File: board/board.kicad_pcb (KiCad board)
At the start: 2 copper layers, 41 parts, among them J2 Conn_01x10, J3 Conn_01x06, J4 Conn_01x02, J7 Conn_01x30, J8 USB_C_Receptacle_USB2.0_16P, J9 Conn_01x02, U2 nPM1300-QEAA, U3 MDBT50Q-P1MV2, U4 TVS_Array, Y1 32k Hz

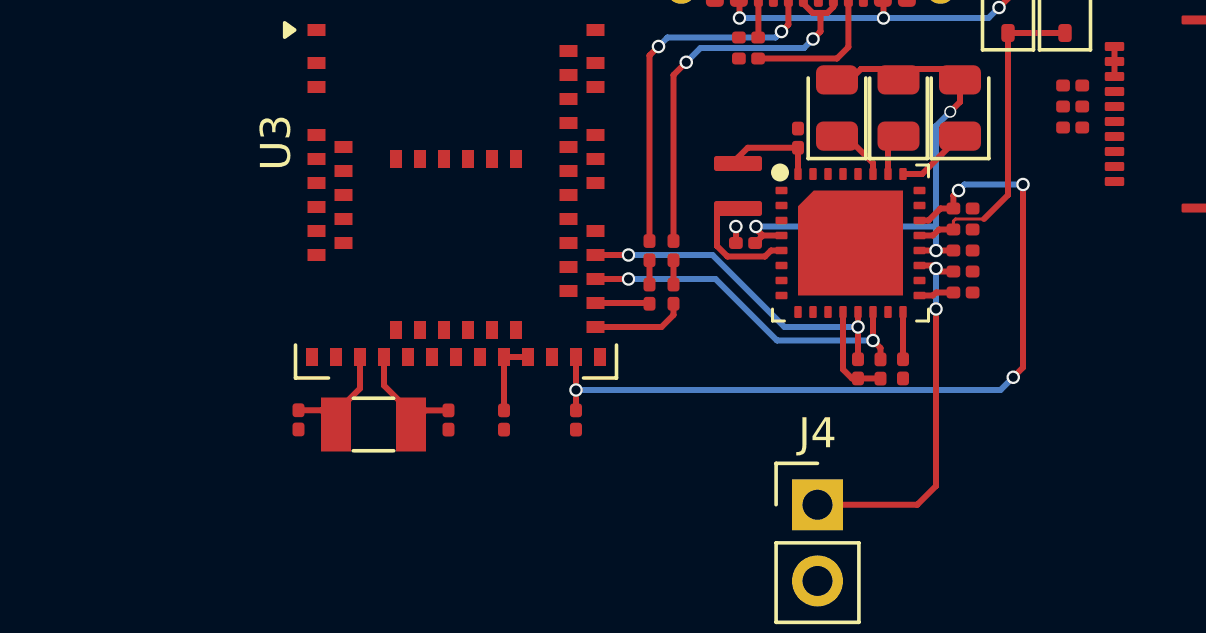
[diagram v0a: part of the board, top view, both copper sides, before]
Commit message: board: pcb move components and traces extending over the edge
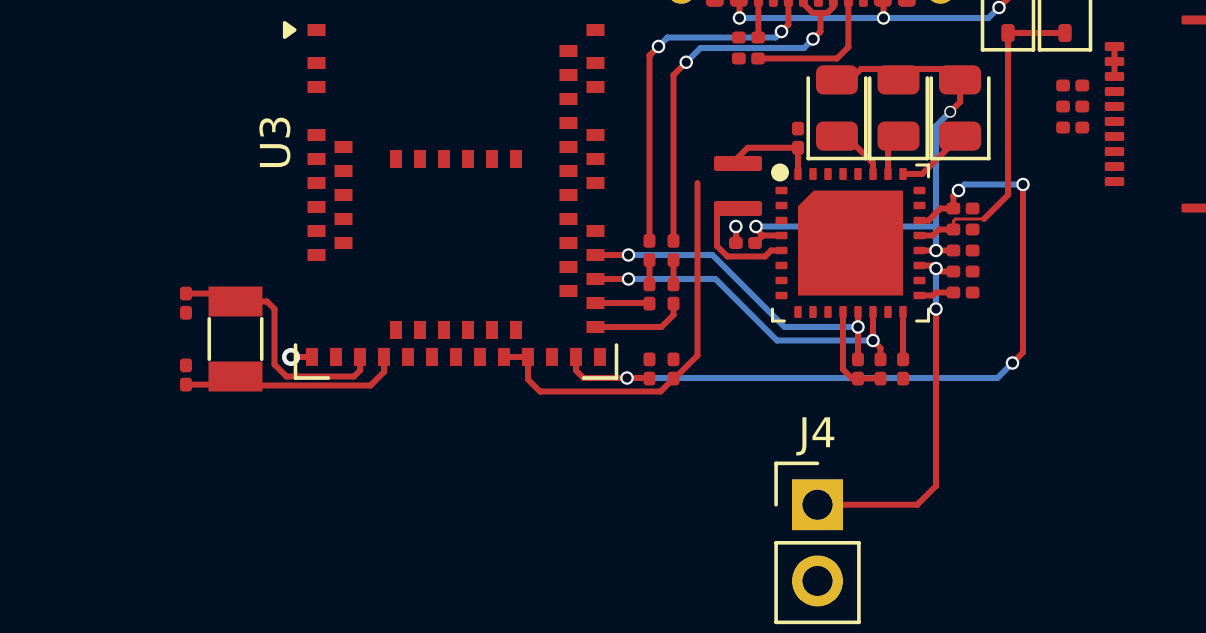
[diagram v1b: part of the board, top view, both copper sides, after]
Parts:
- moved C7 8.88 mm to (90.8, 65.7), turned to 90 degrees
- moved C10 5.90 mm to (107.1, 65.5), turned to -90 degrees
- moved Y1 5.41 mm to (92.5, 64.5), turned to 90 degrees
- moved C8 5.40 mm to (90.8, 63.3)
- moved C9 2.98 mm to (106.3, 65.5), turned to 90 degrees
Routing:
- net +3V3: track 9.22 -> 20.3 mm
- net Net-(U3-P0.00): track 4.03 -> 8.56 mm
- net Net-(U3-P0.01): track 4.07 -> 7.15 mm
- net vbus: track 27.3 -> 26.4 mm
- net GND: track 1.56 -> 2.26 mm, vias 1 -> 2

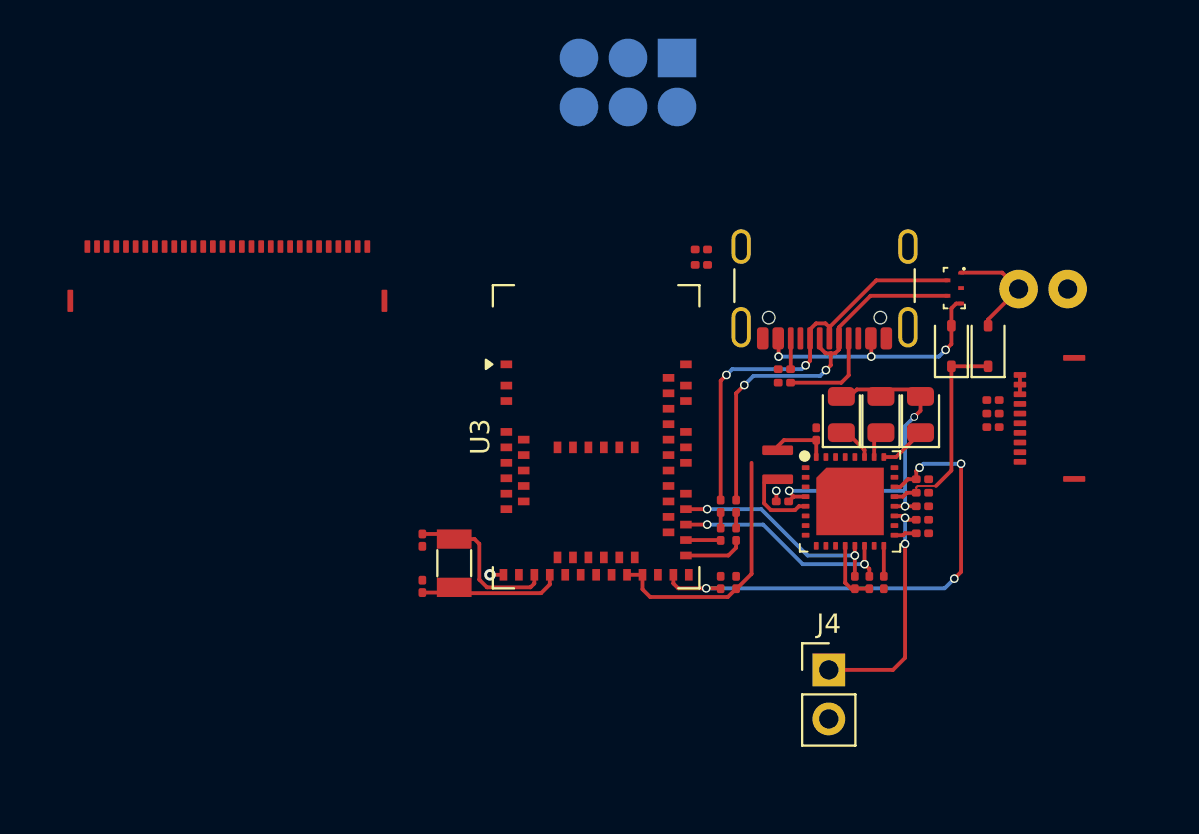
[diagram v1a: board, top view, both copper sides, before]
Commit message: board: pcb add edge cuts
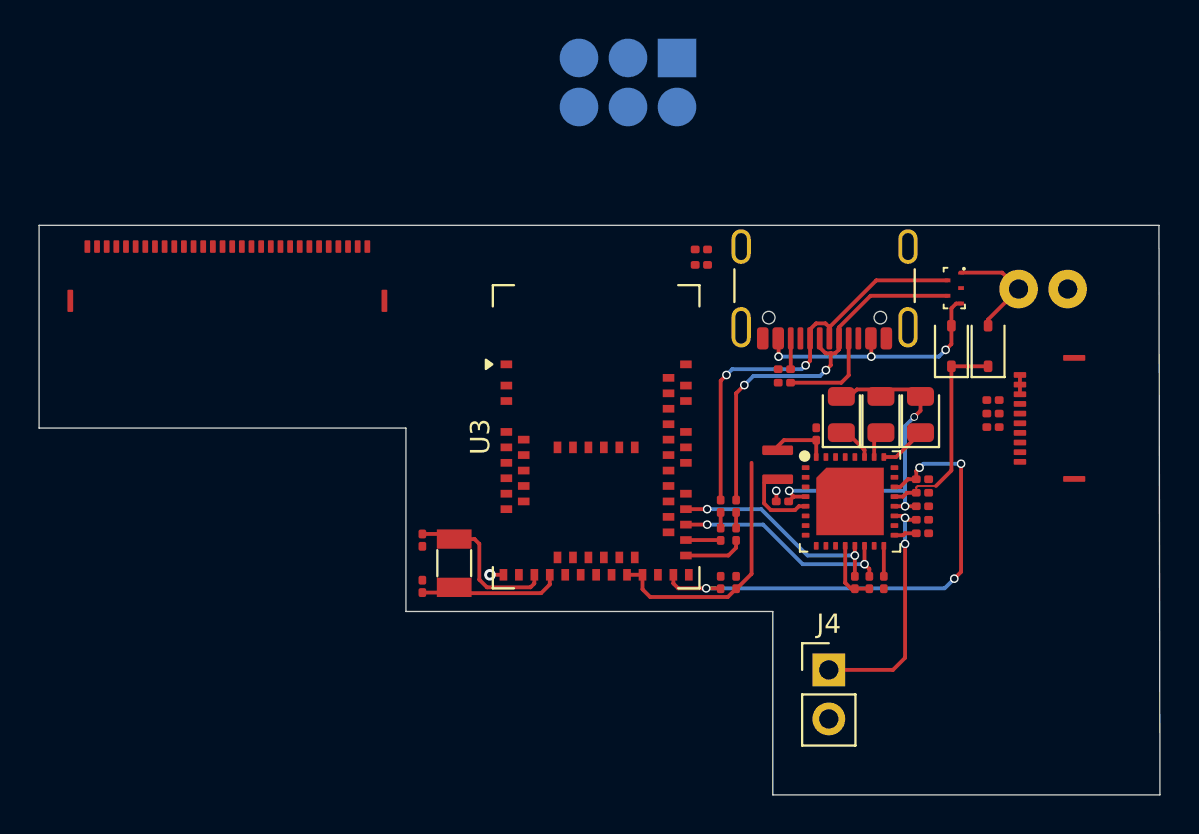
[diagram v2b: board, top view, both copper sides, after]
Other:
- board outline added: 58.1 x 29.5 mm
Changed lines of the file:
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@@
 		(embedded_fonts no)
+	)
+	(gr_poly
+		(pts
+			(xy 71 47) (xy 71 57.5) (xy 90 57.5) (xy 90 67) (xy 109 67) (xy 109 76.5) (xy 129.05 76.5) (xy 129 47)
+		)
+		(stroke
+			(width 0.05)
+			(type solid)
+		)
+		(fill no)
+		(layer "Edge.Cuts")
 	)
 	(gr_line

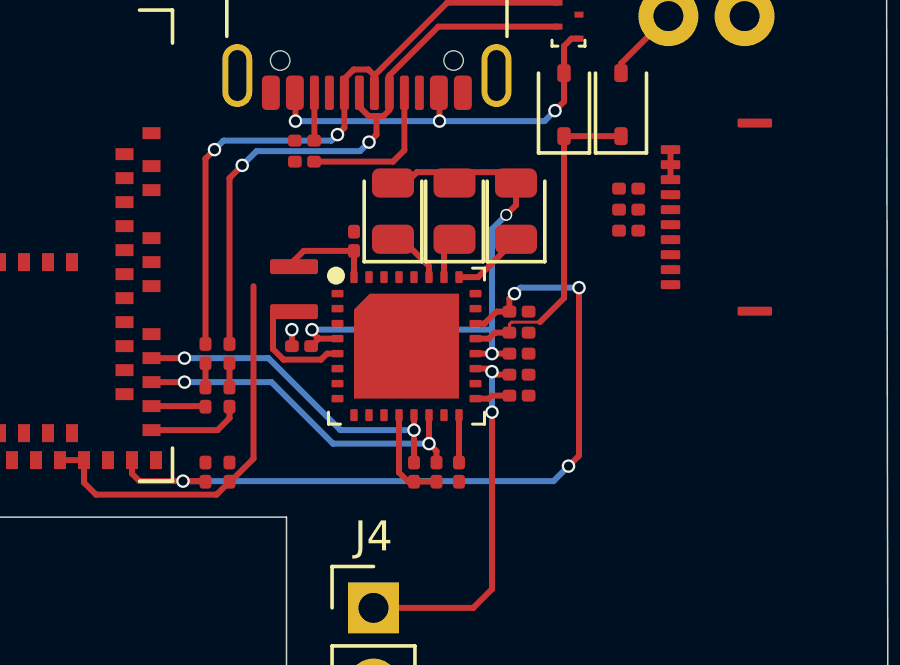
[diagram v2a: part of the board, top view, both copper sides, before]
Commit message: board: pcb route (most of) 3.3V
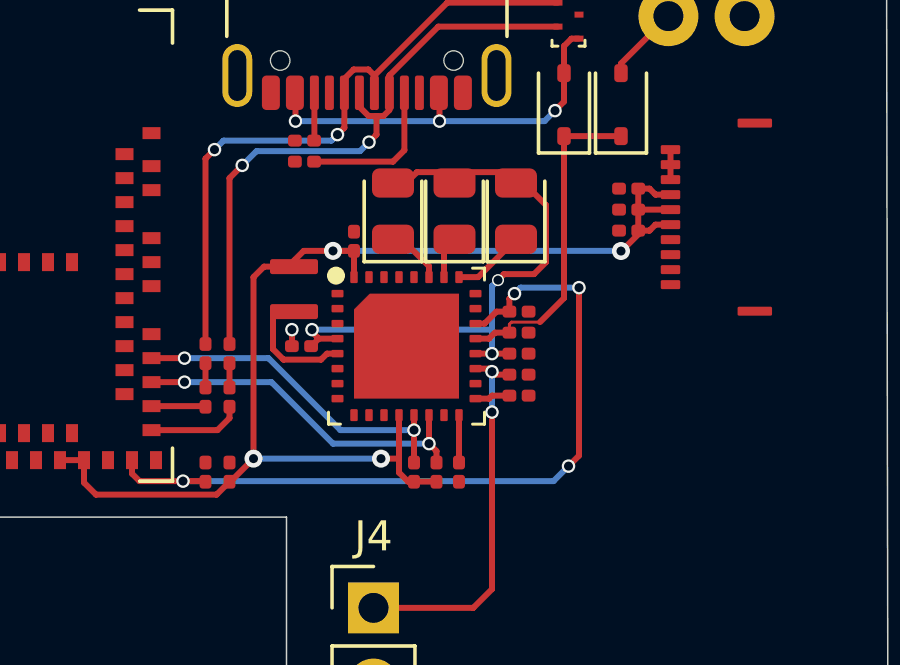
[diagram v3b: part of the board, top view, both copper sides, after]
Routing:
- net +3V3: track 20.3 -> 42.2 mm, vias 0 -> 4
- net vsys: track 18.6 -> 20.2 mm
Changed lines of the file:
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@@
 		)
 		(fp_text user "${REFERENCE}"
-			(at -1.05 3.4 0)
+			(at -2.1 3.4 0)
 			(unlocked yes)
 			(layer "F.Fab")
@@
 	)
 	(segment
-		(start 116.2875 55.5)
-		(end 116.65 55.8625)
+		(start 116.25 58.9)
+		(end 117.25 58.9)
 		(width 0.2)
 		(layer "F.Cu")
@@
 	)
 	(segment
-		(start 116.325 56.925)
-		(end 116.65 56.6)
+		(start 116.2875 55.5)
+		(end 116.65 55.8625)
 		(width 0.2)
 		(layer "F.Cu")
@@
 	)
 	(segment
-		(start 116.65 56.6)
+		(start 117.65 58.5)
+		(end 117.65 56.6)
+		(width 0.2)
+		(layer "F.Cu")
+		(net 6)
+	)
+	(segment
+		(start 117.65 56.6)
+		(end 116.9125 55.8625)
+		(width 0.2)
+		(layer "F.Cu")
+		(net 6)
+	)
+	(segment
+		(start 116.9125 55.8625)
 		(end 116.65 55.8625)
 		(width 0.2)
@@
 	)
 	(segment
+		(start 116.05 59.1)
+		(end 116.25 58.9)
+		(width 0.2)
+		(layer "F.Cu")
+		(net 6)
+	)
+	(segment
+		(start 117.25 58.9)
+		(end 117.65 58.5)
+		(width 0.2)
+		(layer "F.Cu")
+		(net 6)
+	)
+	(segment
 		(start 109.825 61.3)
 		(end 110.075 61.05)
@@
 	)
 	(via
-		(at 116.325 56.925)
+		(at 116.05 59.1)
 		(size 0.4)
 		(drill 0.3)
@@
 	)
 	(segment
-		(start 116.325 56.925)
-		(end 115.85 57.4)
+		(start 116.05 59.1)
+		(end 115.85 59.3)
 		(width 0.2)
 		(layer "B.Cu")
@@
 	)
 	(segment
-		(start 115.85 57.4)
+		(start 109.85 60.75)
 		(end 115.85 60.75)
 		(width 0.2)
@@
 	)
 	(segment
-		(start 109.85 60.75)
+		(start 115.85 59.3)
 		(end 115.85 60.75)
 		(width 0.2)
@@
 	)
 	(segment
-		(start 107.13 65.82)
-		(end 107.9 65.05)
+		(start 120.725 56.05)
+		(end 120.725 57.45)
+		(width 0.2)
+		(layer "F.Cu")
+		(net 46)
+	)
+	(segment
+		(start 120.725 57.575)
+		(end 120.725 57.45)
+		(width 0.2)
+		(layer "F.Cu")
+		(net 46)
+	)
+	(segment
+		(start 109.25 58.65)
+		(end 108.25 58.65)
+		(width 0.2)
+		(layer "F.Cu")
+		(net 46)
+	)
+	(segment
+		(start 121.1 56.05)
+		(end 121.3 56.25)
+		(width 0.2)
+		(layer "F.Cu")
+		(net 46)
+	)
+	(segment
+		(start 120.725 56.05)
+		(end 121.1 56.05)
 		(width 0.2)
 		(layer "F.Cu")
@@
 	)
 	(segment
+		(start 112.15 65.05)
+		(end 112.75 65.05)
+		(width 0.2)
+		(layer "F.Cu")
+		(net 46)
+	)
+	(segment
 		(start 109.575 58.125)
 		(end 109.25 58.45)
@@
 	)
 	(segment
+		(start 121.3 56.25)
+		(end 121.8 56.25)
+		(width 0.2)
+		(layer "F.Cu")
+		(net 46)
+	)
+	(segment
 		(start 102.25 65.1)
 		(end 102.25 65.85)
@@
 	)
 	(segment
+		(start 120.15 58.15)
+		(end 120.725 57.575)
+		(width 0.2)
+		(layer "F.Cu")
+		(net 46)
+	)
+	(segment
+		(start 108.25 58.65)
+		(end 107.9 59)
+		(width 0.2)
+		(layer "F.Cu")
+		(net 46)
+	)
+	(segment
 		(start 109.25 58.45)
 		(end 109.25 58.65)
@@
 	)
 	(segment
-		(start 113.050001 65.815)
-		(end 114 65.815)
+		(start 107.13 65.82)
+		(end 107.1 65.82)
 		(width 0.2)
 		(layer "F.Cu")
@@
 	)
 	(segment
-		(start 107.9 65.05)
-		(end 107.9 59.3)
+		(start 113.050001 65.815)
+		(end 114 65.815)
 		(width 0.2)
 		(layer "F.Cu")
@@
 	(segment
 		(start 111.25 58.125)
-		(end 109.575 58.125)
+		(end 110.55 58.125)
 		(width 0.2)
 		(layer "F.Cu")
@@
 	)
 	(segment
-		(start 107.1 65.82)
+		(start 107.9 65.05)
 		(end 107.13 65.82)
 		(width 0.2)
@@
 	)
 	(segment
+		(start 112.75 63.6)
+		(end 112.75 65.05)
+		(width 0.2)
+		(layer "F.Cu")
+		(net 46)
+	)
+	(segment
+		(start 121.1 57.45)
+		(end 121.3 57.25)
+		(width 0.2)
+		(layer "F.Cu")
+		(net 46)
+	)
+	(segment
+		(start 110.55 58.125)
+		(end 109.575 58.125)
+		(width 0.2)
+		(layer "F.Cu")
+		(net 46)
+	)
+	(segment
+		(start 120.725 56.75)
+		(end 121.8 56.75)
+		(width 0.2)
+		(layer "F.Cu")
+		(net 46)
+	)
+	(segment
 		(start 106.67 66.25)
 		(end 107.1 65.82)
@@
 	)
 	(segment
+		(start 107.9 59)
+		(end 107.9 65.05)
+		(width 0.2)
+		(layer "F.Cu")
+		(net 46)
+	)
+	(segment
+		(start 121.3 57.25)
+		(end 121.8 57.25)
+		(width 0.2)
+		(layer "F.Cu")
+		(net 46)
+	)
+	(segment
 		(start 112.75 65.514999)
 		(end 113.050001 65.815)
@@
 	)
 	(segment
-		(start 112.75 63.6)
+		(start 112.75 65.05)
 		(end 112.75 65.514999)
 		(width 0.2)
@@
 		(net 46)
 	)
+	(segment
+		(start 120.725 57.45)
+		(end 121.1 57.45)
+		(width 0.2)
+		(layer "F.Cu")
+		(net 46)
+	)
+	(via
+		(at 110.55 58.125)
+		(size 0.6)
+		(drill 0.3)
+		(layers "F.Cu" "B.Cu")
+		(net 46)
+	)
+	(via
+		(at 112.15 65.05)
+		(size 0.6)
+		(drill 0.3)
+		(layers "F.Cu" "B.Cu")
+		(net 46)
+	)
+	(via
+		(at 107.9 65.05)
+		(size 0.6)
+		(drill 0.3)
+		(layers "F.Cu" "B.Cu")
+		(net 46)
+	)
+	(via
+		(at 120.15 58.13)
+		(size 0.6)
+		(drill 0.3)
+		(layers "F.Cu" "B.Cu")
+		(net 46)
+	)
+	(segment
+		(start 110.55 58.125)
+		(end 120.125 58.125)
+		(width 0.2)
+		(layer "B.Cu")
+		(net 46)
+	)
+	(segment
+		(start 120.125 58.125)
+		(end 120.15 58.15)
+		(width 0.2)
+		(layer "B.Cu")
+		(net 46)
+	)
+	(segment
+		(start 107.9 65.05)
+		(end 112.15 65.05)
+		(width 0.2)
+		(layer "B.Cu")
+		(net 46)
+	)
